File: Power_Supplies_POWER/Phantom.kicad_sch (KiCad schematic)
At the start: 18 parts, among them IC1 NCP731ADNADJR2G, IC2 LT8338

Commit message: fixed a lot of stuff
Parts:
- added C5: 0.01uF, Capacitor_SMD:C_0402_1005Metric, symbol Device:C
- C52: value 2.2uF -> 0.1uF
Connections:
- net GND: now also C5.1
- net at IC2.9 (CTRL), R40.2, R41.1: now also C5.2
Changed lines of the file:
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@@
 	)
 	(junction
+		(at 185.42 59.69)
+		(diameter 0)
+		(color 0 0 0 0)
+	)
+	(junction
 		(at 167.64 109.22)
 		(diameter 0)
@@
 	(wire
 		(pts
+			(xy 185.42 59.69) (xy 195.58 59.69)
+		)
+		(stroke
+			(width 0)
+			(type default)
+		)
+	)
+	(wire
+		(pts
 			(xy 115.57 116.84) (xy 115.57 119.38)
 		)
@@
 	(wire
 		(pts
-			(xy 180.34 59.69) (xy 195.58 59.69)
+			(xy 180.34 59.69) (xy 185.42 59.69)
 		)
 		(stroke
@@
 			)
 		)
-		(property "Value" "2.2uF"
+		(property "Value" "0.1uF"
 			(at 163.83 38.1 90)
 			(effects
@@
 	(symbol
 		(lib_id "power:GND")
+		(at 185.42 67.31 0)
+		(unit 1)
+		(exclude_from_sim no)
+		(in_bom yes)
+		(on_board no)
+		(dnp no)
+		(fields_autoplaced yes)
+		(property "Reference" "#PWR07"
+			(at 185.42 73.66 0)
+			(effects
+				(font
+					(size 1.27 1.27)
+				)
+				(hide yes)
+			)
+		)
+		(property "Value" "GND"
+			(at 185.42 72.39 0)
+			(effects
+				(font
+					(size 1.27 1.27)
+				)
+			)
+		)
+		(property "Footprint" ""
+			(at 185.42 67.31 0)
+			(effects
+				(font
+					(size 1.27 1.27)
+				)
+				(hide yes)
+			)
+		)
+		(property "Datasheet" ""
+			(at 185.42 67.31 0)
+			(effects
+				(font
+					(size 1.27 1.27)
+				)
+				(hide yes)
+			)
+		)
+		(property "Description" "Power symbol creates a global label with name \"GND\" , ground"
+			(at 185.42 67.31 0)
+			(effects
+				(font
+					(size 1.27 1.27)
+				)
+				(hide yes)
+			)
+		)
+		(pin "1"
+		)
+		(instances
+			(project "Power_Supplies_Copy"
+				(path "/5266cf9e-da90-4c53-80fd-cf3dbed42632/873b4819-32e6-40de-93d6-23cb6a01b934"
+					(reference "#PWR07")
+					(unit 1)
+				)
+			)
+		)
+	)
+	(symbol
+		(lib_id "power:GND")
 		(at 109.22 116.84 0)
 		(unit 1)
@@
 					(unit 1)
 				)
+			)
+		)
+	)
+	(symbol
+		(lib_id "Device:C")
+		(at 185.42 63.5 180)
+		(unit 1)
+		(exclude_from_sim no)
+		(in_bom yes)
+		(on_board yes)
+		(dnp no)
+		(property "Reference" "C5"
+			(at 189.23 62.2299 0)
+			(effects
+				(font
+					(size 1.27 1.27)
+				)
+				(justify right)
+			)
+		)
+		(property "Value" "0.01uF"
+			(at 187.706 65.532 0)
+			(effects
+				(font
+					(size 1.27 1.27)
+				)
+				(justify right)
+			)
+		)
+		(property "Footprint" "Capacitor_SMD:C_0402_1005Metric"
+			(at 184.4548 59.69 0)
+			(effects
+				(font
+					(size 1.27 1.27)
+				)
+				(hide yes)
+			)
+		)
+		(property "Datasheet" "~"
+			(at 185.42 63.5 0)
+			(effects
+				(font
+					(size 1.27 1.27)
+				)
+				(hide yes)
+			)
+		)
+		(property "Description" "Unpolarized capacitor"
+			(at 185.42 63.5 0)
+			(effects
+				(font
+					(size 1.27 1.27)
+				)
+				(hide yes)
+			)
+		)
+		(pin "1"
+		)
+		(pin "2"
+		)
+		(instances
+			(project "Power_Supplies_Copy"
+				(path "/5266cf9e-da90-4c53-80fd-cf3dbed42632/873b4819-32e6-40de-93d6-23cb6a01b934"
+					(reference "C5")
+					(unit 1)
+				)

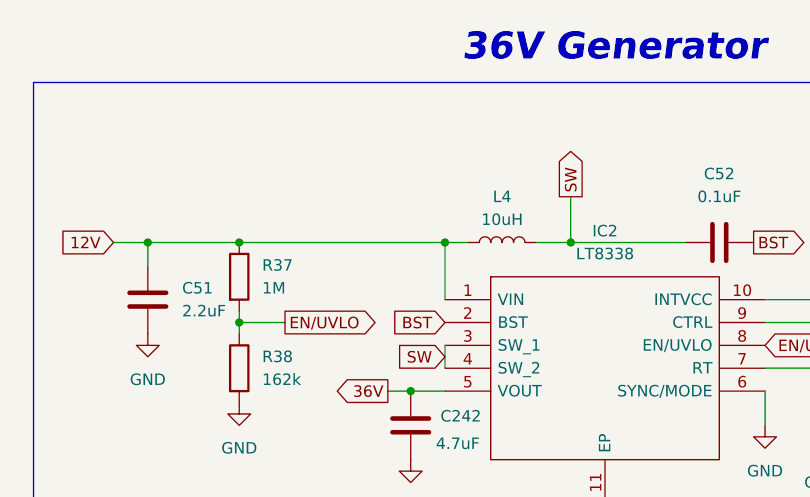
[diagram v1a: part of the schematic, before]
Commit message: fixed power board problems/...
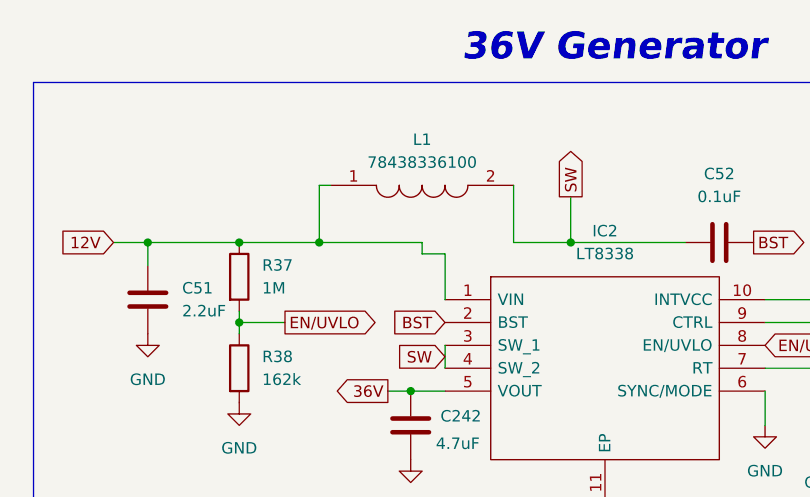
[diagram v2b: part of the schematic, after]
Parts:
- removed L4: 10uH, Inductor_SMD:L_0805_2012Metric, symbol Device:L
- added L1: 78438336100, SamacSys_Parts:INDC3030X200N, symbol SamacSys_Parts:78438336100
- C5: footprint Capacitor_SMD:C_0402_1005Metric -> Capacitor_SMD:C_0402_1005Metric_Pad0.74x0.62mm_HandSolder
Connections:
- net 12V: now also L1.1
- net SW: now also L1.2
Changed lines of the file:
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@@
 	)
 	(junction
-		(at 109.22 109.22)
+		(at 119.38 43.18)
 		(diameter 0)
 		(color 0 0 0 0)
 	)
 	(junction
-		(at 185.42 59.69)
+		(at 109.22 109.22)
 		(diameter 0)
 		(color 0 0 0 0)
 	)
 	(junction
-		(at 167.64 109.22)
+		(at 185.42 59.69)
 		(diameter 0)
 		(color 0 0 0 0)
 	)
 	(junction
-		(at 100.33 43.18)
+		(at 167.64 109.22)
 		(diameter 0)
 		(color 0 0 0 0)
 	)
 	(junction
-		(at 133.35 43.18)
+		(at 100.33 43.18)
 		(diameter 0)
 		(color 0 0 0 0)
@@
 	(wire
 		(pts
-			(xy 143.51 43.18) (xy 147.32 43.18)
+			(xy 168.91 52.07) (xy 180.34 52.07)
 		)
 		(stroke
@@
 	(wire
 		(pts
-			(xy 168.91 52.07) (xy 180.34 52.07)
+			(xy 100.33 43.18) (xy 110.49 43.18)
 		)
 		(stroke
@@
 	(wire
 		(pts
-			(xy 100.33 43.18) (xy 110.49 43.18)
+			(xy 119.38 43.18) (xy 130.81 43.18)
 		)
 		(stroke
@@
 	(wire
 		(pts
-			(xy 133.35 43.18) (xy 133.35 49.53)
+			(xy 130.81 43.18) (xy 130.81 44.45)
 		)
 		(stroke
@@
 	(wire
 		(pts
-			(xy 125.73 111.76) (xy 125.73 119.38)
+			(xy 130.81 44.45) (xy 133.35 44.45)
 		)
 		(stroke
@@
 	(wire
 		(pts
-			(xy 109.22 109.22) (xy 115.57 109.22)
+			(xy 133.35 44.45) (xy 133.35 49.53)
 		)
 		(stroke
@@
 	(wire
 		(pts
-			(xy 171.45 109.22) (xy 167.64 109.22)
+			(xy 140.97 43.18) (xy 140.97 36.83)
 		)
 		(stroke
@@
 	(wire
 		(pts
-			(xy 163.83 114.3) (xy 163.83 119.38)
+			(xy 140.97 43.18) (xy 147.32 43.18)
 		)
 		(stroke
@@
 	(wire
 		(pts
-			(xy 115.57 119.38) (xy 121.92 119.38)
+			(xy 125.73 111.76) (xy 125.73 119.38)
 		)
 		(stroke
@@
 	(wire
 		(pts
-			(xy 110.49 52.07) (xy 115.57 52.07)
+			(xy 109.22 109.22) (xy 115.57 109.22)
 		)
 		(stroke
@@
 	(wire
 		(pts
-			(xy 133.35 43.18) (xy 135.89 43.18)
+			(xy 171.45 109.22) (xy 167.64 109.22)
+		)
+		(stroke
+			(width 0)
+			(type default)
+		)
+	)
+	(wire
+		(pts
+			(xy 163.83 114.3) (xy 163.83 119.38)
+		)
+		(stroke
+			(width 0)
+			(type default)
+		)
+	)
+	(wire
+		(pts
+			(xy 115.57 119.38) (xy 121.92 119.38)
+		)
+		(stroke
+			(width 0)
+			(type default)
+		)
+	)
+	(wire
+		(pts
+			(xy 110.49 52.07) (xy 115.57 52.07)
 		)
 		(stroke
@@
 	(wire
 		(pts
+			(xy 120.65 36.83) (xy 119.38 36.83)
+		)
+		(stroke
+			(width 0)
+			(type default)
+		)
+	)
+	(wire
+		(pts
 			(xy 161.29 114.3) (xy 163.83 114.3)
 		)
@@
 	(wire
 		(pts
-			(xy 195.58 57.15) (xy 195.58 59.69)
+			(xy 119.38 36.83) (xy 119.38 43.18)
 		)
 		(stroke
@@
 	(wire
 		(pts
-			(xy 185.42 59.69) (xy 195.58 59.69)
+			(xy 195.58 57.15) (xy 195.58 59.69)
 		)
 		(stroke
@@
 	(wire
 		(pts
-			(xy 115.57 116.84) (xy 115.57 119.38)
+			(xy 185.42 59.69) (xy 195.58 59.69)
 		)
 		(stroke
@@
 	(wire
 		(pts
-			(xy 110.49 43.18) (xy 133.35 43.18)
+			(xy 115.57 116.84) (xy 115.57 119.38)
 		)
 		(stroke
@@
 	(wire
 		(pts
+			(xy 110.49 43.18) (xy 119.38 43.18)
+		)
+		(stroke
+			(width 0)
+			(type default)
+		)
+	)
+	(wire
+		(pts
 			(xy 133.35 54.61) (xy 133.35 57.15)
 		)
@@
 	)
 	(symbol
+		(lib_id "SamacSys_Parts:78438336100")
+		(at 120.65 36.83 0)
+		(unit 1)
+		(exclude_from_sim no)
+		(in_bom yes)
+		(on_board yes)
+		(dnp no)
+		(fields_autoplaced yes)
+		(property "Reference" "L1"
+			(at 130.81 31.75 0)
+			(effects
+				(font
+					(size 1.27 1.27)
+				)
+			)
+		)
+		(property "Value" "78438336100"
+			(at 130.81 34.29 0)
+			(effects
+				(font
+					(size 1.27 1.27)
+				)
+			)
+		)
+		(property "Footprint" "SamacSys_Parts:INDC3030X200N"
+			(at 137.16 35.56 0)
+			(effects
+				(font
+					(size 1.27 1.27)
+				)
+				(justify left)
+				(hide yes)
+			)
+		)
+		(property "Datasheet" "https://www.we-online.com/catalog/datasheet/78438336100.pdf"
+			(at 137.16 38.1 0)
+			(effects
+				(font
+					(size 1.27 1.27)
+				)
+				(justify left)
+				(hide yes)
+			)
+		)
+		(property "Description" "Power Inductors - SMD WE-MAIA SMD AEC-Q200 10.0uH 1.2A 322mOhm"
+			(at 120.65 36.83 0)
+			(effects
+				(font
+					(size 1.27 1.27)
+				)
+				(hide yes)
+			)
+		)
+		(property "Description_1" "Power Inductors - SMD WE-MAIA SMD AEC-Q200 10.0uH 1.2A 322mOhm"
+			(at 137.16 40.64 0)
+			(effects
+				(font
+					(size 1.27 1.27)
+				)
+				(justify left)
+				(hide yes)
+			)
+		)
+		(property "Height" "2"
+			(at 137.16 43.18 0)
+			(effects
+				(font
+					(size 1.27 1.27)
+				)
+				(justify left)
+				(hide yes)
+			)
+		)
+		(property "Manufacturer_Name" "Wurth Elektronik"
+			(at 137.16 45.72 0)
+			(effects
+				(font
+					(size 1.27 1.27)
+				)
+				(justify left)
+				(hide yes)
+			)
+		)
+		(property "Manufacturer_Part_Number" "78438336100"
+			(at 137.16 48.26 0)
+			(effects
+				(font
+					(size 1.27 1.27)
+				)
+				(justify left)
+				(hide yes)
+			)
+		)
+		(property "Mouser Part Number" "710-78438336100"
+			(at 137.16 50.8 0)
+			(effects
+				(font
+					(size 1.27 1.27)
+				)
+				(justify left)
+				(hide yes)
+			)
+		)
+		(property "Mouser Price/Stock" "https://www.mouser.co.uk/ProductDetail/Wurth-Elektronik/78438336100?qs=r5DSvlrkXmLcJRTgODo0FA%3D%3D"
+			(at 137.16 53.34 0)
+			(effects
+				(font
+					(size 1.27 1.27)
+				)
+				(justify left)
+				(hide yes)
+			)
+		)
+		(property "Arrow Part Number" ""
+			(at 137.16 55.88 0)
+			(effects
+				(font
+					(size 1.27 1.27)
+				)
+				(justify left)
+				(hide yes)
+			)
+		)
+		(property "Arrow Price/Stock" ""
+			(at 137.16 58.42 0)
+			(effects
+				(font
+					(size 1.27 1.27)
+				)
+				(justify left)
+				(hide yes)
+			)
+		)
+		(pin "2"
+		)
+		(pin "1"
+		)
+		(instances
+			(project ""
+				(path "/5266cf9e-da90-4c53-80fd-cf3dbed42632/873b4819-32e6-40de-93d6-23cb6a01b934"
+					(reference "L1")
+					(unit 1)
+				)
+			)
+		)
+	)
+	(symbol
 		(lib_id "Device:C")
 		(at 163.83 43.18 90)
@@
 	)
 	(symbol
-		(lib_id "Device:L")
-		(at 139.7 43.18 90)
-		(unit 1)
-		(exclude_from_sim no)
-		(in_bom yes)
-		(on_board yes)
-		(dnp no)
-		(fields_autoplaced yes)
-		(property "Reference" "L4"
-			(at 139.7 38.1 90)
-			(effects
-				(font
-					(size 1.27 1.27)
-				)
-			)
-		)
-		(property "Value" "10uH"
-			(at 139.7 40.64 90)
-			(effects
-				(font
-					(size 1.27 1.27)
-				)
-			)
-		)
-		(property "Footprint" "Inductor_SMD:L_0805_2012Metric"
-			(at 139.7 43.18 0)
-			(effects
-				(font
-					(size 1.27 1.27)
-				)
-				(hide yes)
-			)
-		)
-		(property "Datasheet" "~"
-			(at 139.7 43.18 0)
-			(effects
-				(font
-					(size 1.27 1.27)
-				)
-				(hide yes)
-			)
-		)
-		(property "Description" "Inductor"
-			(at 139.7 43.18 0)
-			(effects
-				(font
-					(size 1.27 1.27)
-				)
-				(hide yes)
-			)
-		)
-		(pin "2"
-		)
-		(pin "1"
-		)
-		(instances
-			(project "Power_Supplies"
-				(path "/5266cf9e-da90-4c53-80fd-cf3dbed42632/873b4819-32e6-40de-93d6-23cb6a01b934"
-					(reference "L4")
-					(unit 1)
-				)
-			)
-		)
-	)
-	(symbol
 		(lib_id "Device:C")
 		(at 185.42 63.5 180)
@@
 			)
 		)
-		(property "Footprint" "Capacitor_SMD:C_0402_1005Metric"
+		(property "Footprint" "Capacitor_SMD:C_0402_1005Metric_Pad0.74x0.62mm_HandSolder"
 			(at 184.4548 59.69 0)
 			(effects

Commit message: aaaah (cooked)
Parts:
- removed C242: 4.7uF, Capacitor_SMD:C_0805_2012Metric_Pad1.18x1.45mm_HandSolder, symbol Device:C
- removed C5: 0.01uF, Capacitor_SMD:C_0402_1005Metric_Pad0.74x0.62mm_HandSolder, symbol Device:C
- removed C51, C53: 2.2uF, Capacitor_SMD:C_0805_2012Metric_Pad1.18x1.45mm_HandSolder, symbol Device:C
- removed C52: 0.1uF, Capacitor_SMD:C_0402_1005Metric, symbol Device:C
- removed IC2: LT8338, SamacSys_Parts:SOP50P490X110-11N, symbol SamacSys_Parts:lt8338
- removed L1: 78438336100, SamacSys_Parts:INDC3030X200N, symbol SamacSys_Parts:78438336100
- removed R37, R41: 1M, PCM_Resistor_SMD_AKL:R_0402_1005Metric_Pad0.72x0.64mm_HandSolder, symbol Device:R
- removed R38: 162k, PCM_Resistor_SMD_AKL:R_0402_1005Metric_Pad0.72x0.64mm_HandSolder, symbol Device:R
- removed R39: 40.2k, PCM_Resistor_SMD_AKL:R_0402_1005Metric_Pad0.72x0.64mm_HandSolder, symbol Device:R
- removed R40: 301k, PCM_Resistor_SMD_AKL:R_0402_1005Metric_Pad0.72x0.64mm_HandSolder, symbol Device:R
- added C6: 1.5nF, Capacitor_SMD:C_0805_2012Metric_Pad1.18x1.45mm_HandSolder, symbol Device:C
- added C7: 100uF_25V, Capacitor_SMD:CP_Elec_6.3x5.4, symbol PCM_SL_Capacitors:100uF_50V
- added C8: 330uF_50V, Capacitor_SMD:CP_Elec_10x10.5, symbol PCM_SL_Capacitors:220uF_50V
- added D1: TMBYV10-40FILM, SamacSys_Parts:TMBYV1040FILM, symbol SamacSys_Parts:TMBYV10-40FILM
- added IC3: MC34063ECD-TR, SamacSys_Parts:SOIC127P600X175-8N, symbol SamacSys_Parts:MC34063ECD-TR
- added L2: 180uH, Inductor_SMD:L_Vishay_IHLP-1212, symbol Device:L
- added R3: 180, PCM_Resistor_SMD_AKL:R_0805_2012Metric_Pad1.15x1.40mm_HandSolder, symbol Device:R
- added R4: 0.22, PCM_Resistor_SMD_AKL:R_2512_6332Metric_Pad1.40x3.35mm_HandSolder, symbol Device:R
- added R5: 10k, PCM_Resistor_SMD_AKL:R_0805_2012Metric_Pad1.15x1.40mm_HandSolder, symbol Device:R
- added R6: 280k, PCM_Resistor_SMD_AKL:R_0805_2012Metric_Pad1.15x1.40mm_HandSolder, symbol Device:R
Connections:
- net 12V: now also C7.1, IC3.6 (VCC), R4.1
- net 36V: now also C8.1, D1.1, R6.1
- net GND: now also C6.2, C7.2, C8.2, IC3.2 (SWE), IC3.4 (GND), R5.2
- new net: IC3.5 (CII), R5.1, R6.2
- new net: C6.1, IC3.3 (TC)
- new net: D1.2, IC3.1 (SWC), L2.1
- new net: IC3.7 (IPK), L2.2, R3.2, R4.2
- new net: IC3.8 (DRC), R3.1
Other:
- note added: "Vout = 1.25(1+R2/R1) With R1 = 10k and Vout = 36V, R2 = 280K"
